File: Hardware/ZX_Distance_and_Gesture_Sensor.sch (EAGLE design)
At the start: 48 parts, among them Q1 MMBT2222A, Q2 MOSFET-NCHANNEL2N7002PW, U1 BRM-2508VERT

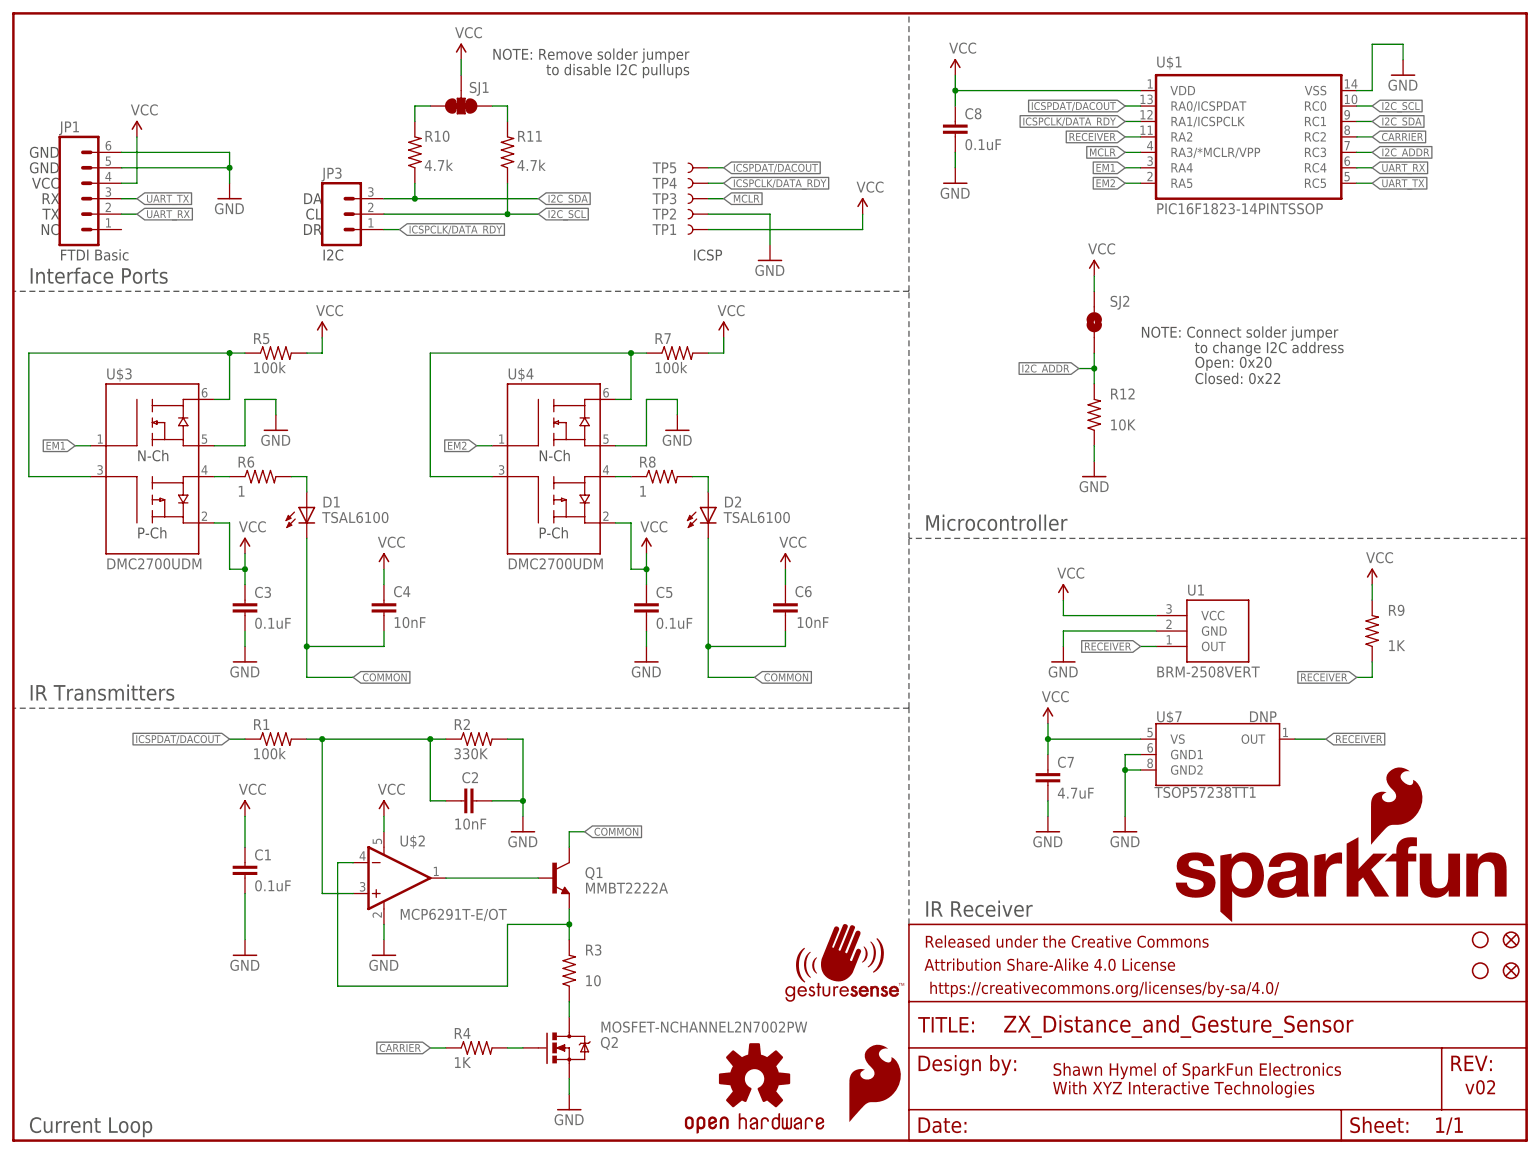
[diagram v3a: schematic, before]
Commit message: Added solder tabs to blinders
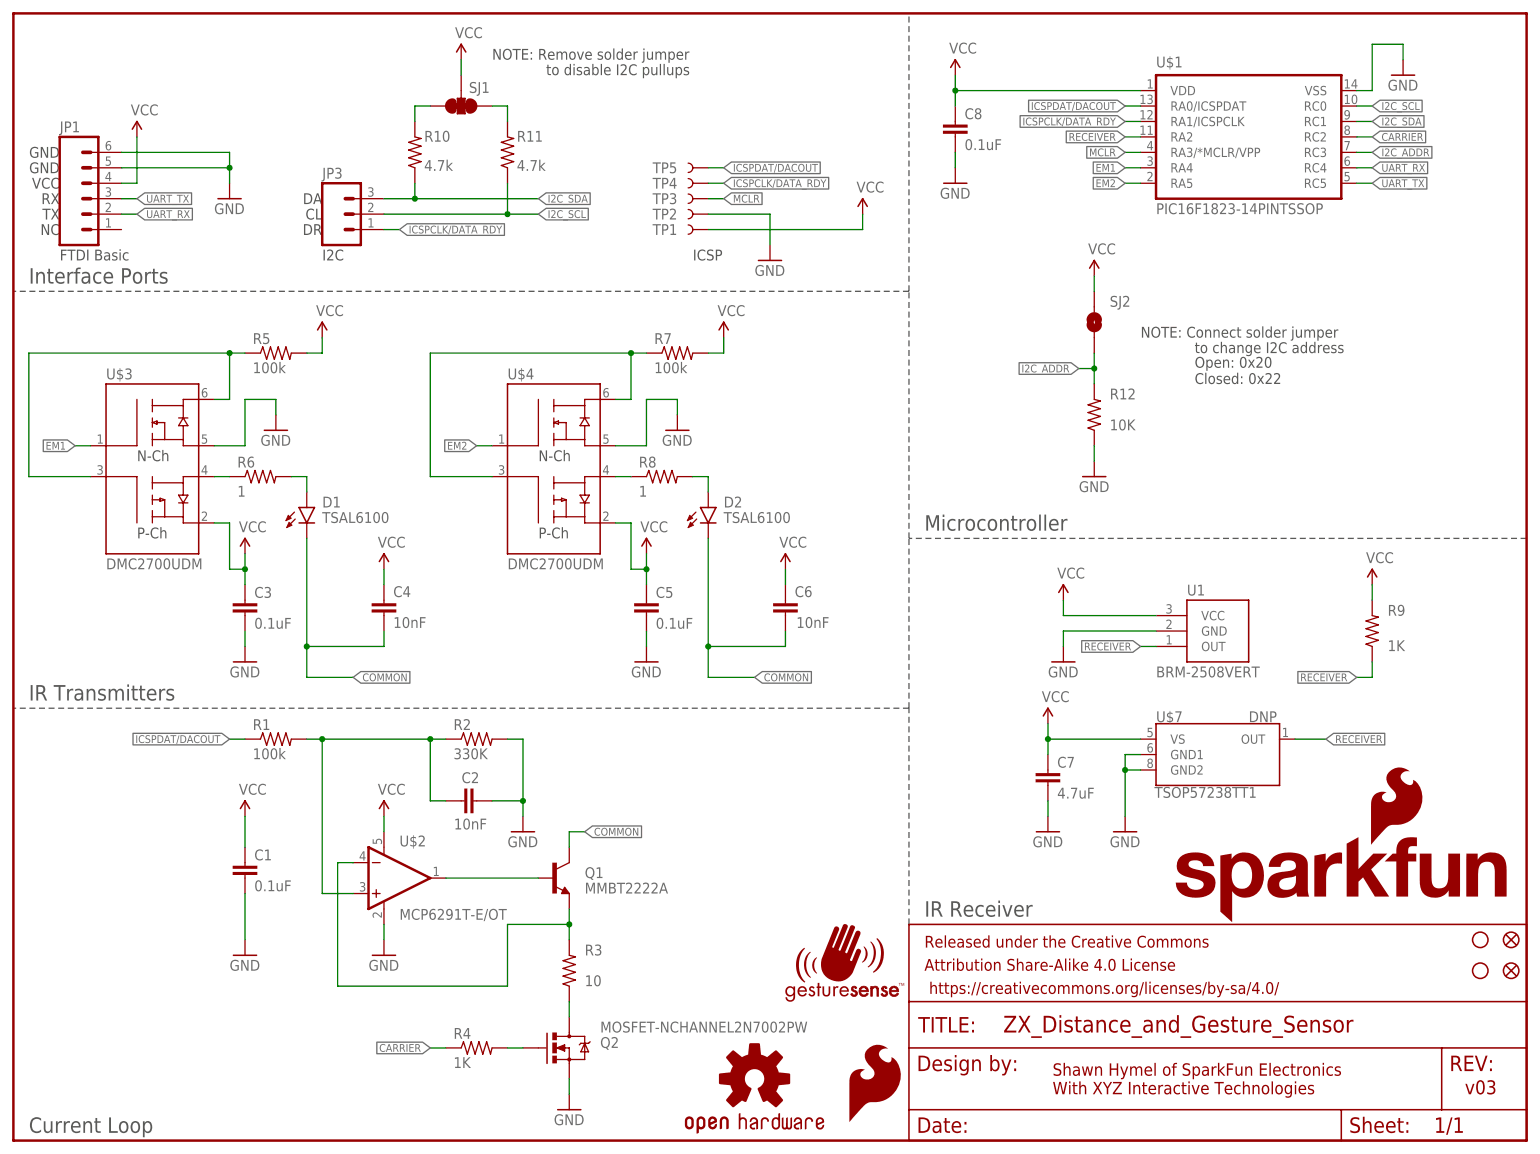
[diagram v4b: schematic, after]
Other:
- note added: "v03"
- note removed: "v02"
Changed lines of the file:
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@@
 <setting verticaltext="up"/>
 </settings>
-<grid distance="0.1" unitdist="inch" unit="inch" style="lines" multiple="1" display="yes" altdistance="0.01" altunitdist="inch" altunit="inch"/>
+<grid distance="0.1" unitdist="inch" unit="inch" style="lines" multiple="1" display="no" altdistance="0.01" altunitdist="inch" altunit="inch"/>
 <layers>
 <layer number="1" name="Top" color="4" fill="1" visible="no" active="no"/>
@@
 <layer number="54" name="bGND_GNDA" color="1" fill="9" visible="no" active="no"/>
 <layer number="56" name="wert" color="7" fill="1" visible="no" active="no"/>
+<layer number="57" name="tCAD" color="7" fill="1" visible="no" active="no"/>
 <layer number="91" name="Nets" color="2" fill="1" visible="yes" active="yes"/>
 <layer number="92" name="Busses" color="1" fill="1" visible="yes" active="yes"/>
@@
 <layer number="97" name="Info" color="7" fill="1" visible="yes" active="yes"/>
 <layer number="98" name="Guide" color="6" fill="1" visible="yes" active="yes"/>
+<layer number="99" name="SpiceOrder" color="7" fill="1" visible="yes" active="yes"/>
 <layer number="100" name="Muster" color="7" fill="1" visible="no" active="no"/>
 <layer number="101" name="Patch_Top" color="12" fill="4" visible="yes" active="yes"/>
@@
 <layer number="108" name="tplace-old" color="10" fill="1" visible="yes" active="yes"/>
 <layer number="109" name="ref-old" color="11" fill="1" visible="yes" active="yes"/>
+<layer number="110" name="fp0" color="7" fill="1" visible="yes" active="yes"/>
+<layer number="111" name="LPC17xx" color="7" fill="1" visible="yes" active="yes"/>
+<layer number="112" name="tSilk" color="7" fill="1" visible="yes" active="yes"/>
 <layer number="116" name="Patch_BOT" color="9" fill="4" visible="yes" active="yes"/>
 <layer number="121" name="_tsilk" color="7" fill="1" visible="yes" active="yes"/>
 <layer number="122" name="_bsilk" color="7" fill="1" visible="yes" active="yes"/>
+<layer number="123" name="tTestmark" color="7" fill="1" visible="yes" active="yes"/>
+<layer number="124" name="bTestmark" color="7" fill="1" visible="yes" active="yes"/>
 <layer number="125" name="_tNames" color="7" fill="1" visible="yes" active="yes"/>
+<layer number="126" name="_bNames" color="7" fill="1" visible="yes" active="yes"/>
+<layer number="127" name="_tValues" color="7" fill="1" visible="yes" active="yes"/>
+<layer number="128" name="_bValues" color="7" fill="1" visible="yes" active="yes"/>
+<layer number="131" name="tAdjust" color="7" fill="1" visible="yes" active="yes"/>
+<layer number="132" name="bAdjust" color="7" fill="1" visible="yes" active="yes"/>
 <layer number="144" name="Drill_legend" color="7" fill="1" visible="yes" active="yes"/>
+<layer number="150" name="Notes" color="7" fill="1" visible="yes" active="yes"/>
 <layer number="151" name="HeatSink" color="7" fill="1" visible="yes" active="yes"/>
+<layer number="152" name="_bDocu" color="7" fill="1" visible="yes" active="yes"/>
+<layer number="153" name="FabDoc1" color="7" fill="1" visible="yes" active="yes"/>
+<layer number="154" name="FabDoc2" color="7" fill="1" visible="yes" active="yes"/>
+<layer number="155" name="FabDoc3" color="7" fill="1" visible="yes" active="yes"/>
 <layer number="199" name="Contour" color="7" fill="1" visible="yes" active="yes"/>
 <layer number="200" name="200bmp" color="1" fill="10" visible="yes" active="yes"/>
@@
 <layer number="223" name="223bmp" color="24" fill="1" visible="no" active="no"/>
 <layer number="224" name="224bmp" color="25" fill="1" visible="no" active="no"/>
+<layer number="248" name="Housing" color="7" fill="1" visible="yes" active="yes"/>
+<layer number="249" name="Edge" color="7" fill="1" visible="yes" active="yes"/>
 <layer number="250" name="Descript" color="3" fill="1" visible="no" active="no"/>
 <layer number="251" name="SMDround" color="12" fill="11" visible="no" active="no"/>
@@
 <sheet>
 <plain>
-<text x="238.76" y="7.62" size="2.286" layer="94">v02</text>
+<text x="238.76" y="7.62" size="2.286" layer="94">v03</text>
 <text x="170.942" y="7.62" size="2.032" layer="94">Shawn Hymel of SparkFun Electronics
 With XYZ Interactive Technologies</text>
